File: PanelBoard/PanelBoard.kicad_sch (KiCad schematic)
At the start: 21 parts, among them J1 Conn_02x08_Odd_Even, J2 Conn_01x04, SW1 SW_SPST, SW2 SW_SPST, SW3 SW_SPST, SW4 SW_SPST

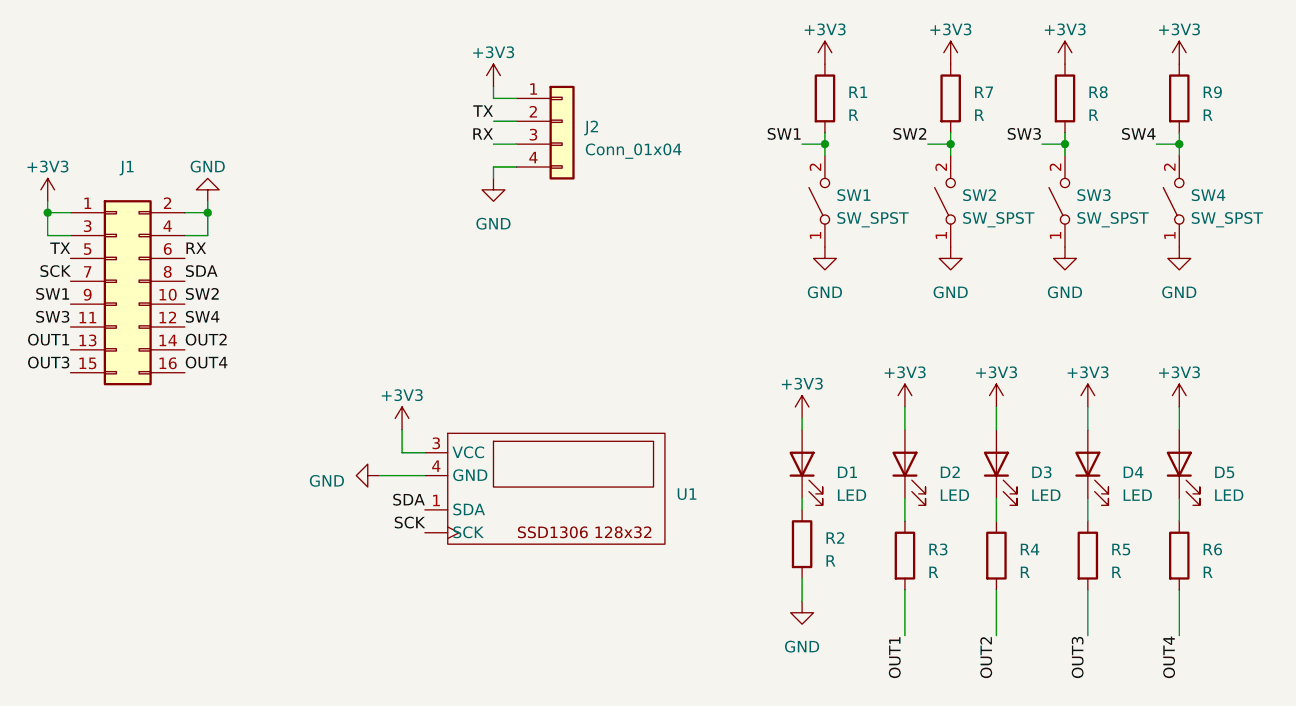
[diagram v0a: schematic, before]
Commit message: panel board pcb designed
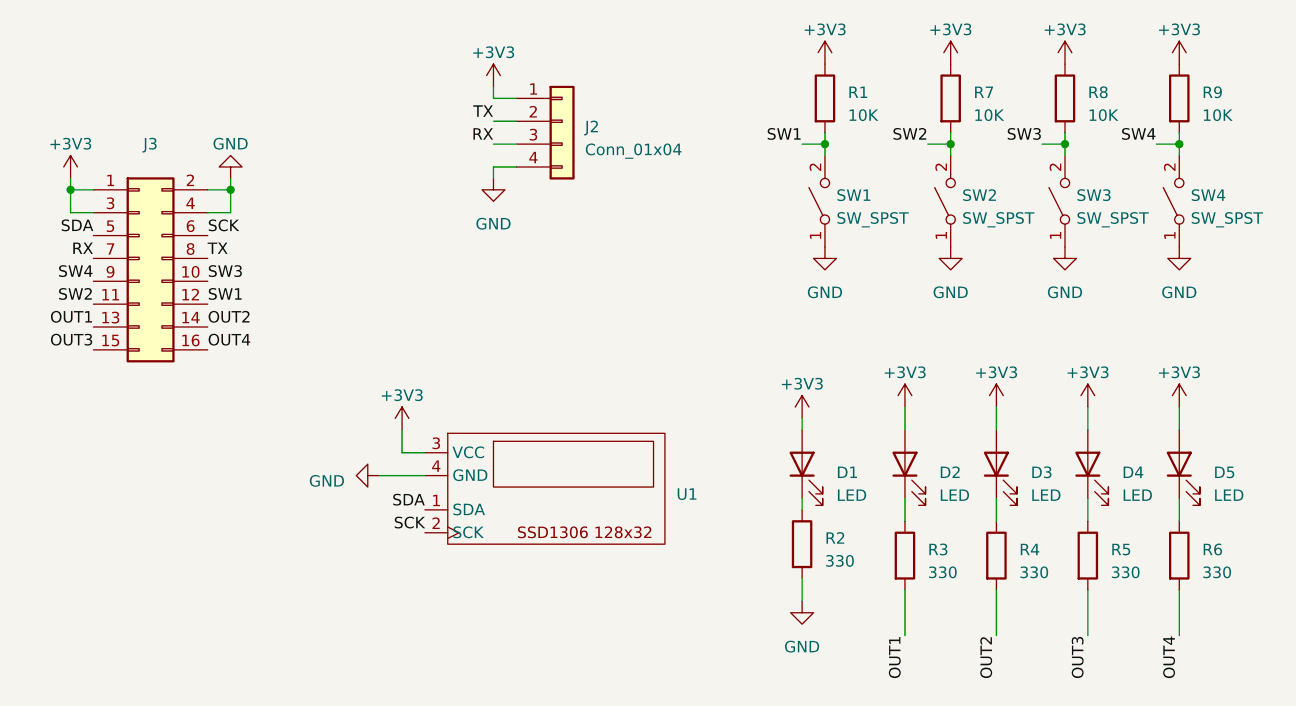
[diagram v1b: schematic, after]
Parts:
- removed J1: Conn_02x08_Odd_Even, Connector_PinHeader_2.54mm:PinHeader_2x08_P2.54mm_Horizontal, symbol Connector_Generic:Conn_02x08_Odd_Even
- added J3: Conn_02x08_Odd_Even, Connector_PinHeader_2.54mm:PinHeader_2x08_P2.54mm_Horizontal, symbol Connector_Generic:Conn_02x08_Odd_Even
- J2: footprint Connector_Molex:Molex_PicoBlade_53048-0410_1x04_P1.25mm_Horizontal -> Connector_PinHeader_2.54mm:PinHeader_1x04_P2.54mm_Vertical
- R1, R7, R8, R9: value R -> 10K
- R2, R3, R4, R5, R6: value R -> 330
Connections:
- net +3V3: now also J3.1 (Pin_1), J3.3 (Pin_3)
- net GND: now also J3.2 (Pin_2), J3.4 (Pin_4)
- net OUT1: now also J3.13 (Pin_13)
- net OUT2: now also J3.14 (Pin_14)
- net OUT3: now also J3.15 (Pin_15)
- net OUT4: now also J3.16 (Pin_16)
- net RX: now also J3.7 (Pin_7)
- net SCK: now also U1.2 (SCK), J3.6 (Pin_6); no longer U1. (SCK)
- net SDA: now also J3.5 (Pin_5)
- net SW1: now also J3.12 (Pin_12)
- net SW2: now also J3.11 (Pin_11)
- net SW3: now also J3.10 (Pin_10)
- net SW4: now also J3.9 (Pin_9)
- net TX: now also J3.8 (Pin_8)
